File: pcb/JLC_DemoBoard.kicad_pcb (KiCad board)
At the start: 2 copper layers, 40.6 x 40.6 mm, 3 parts

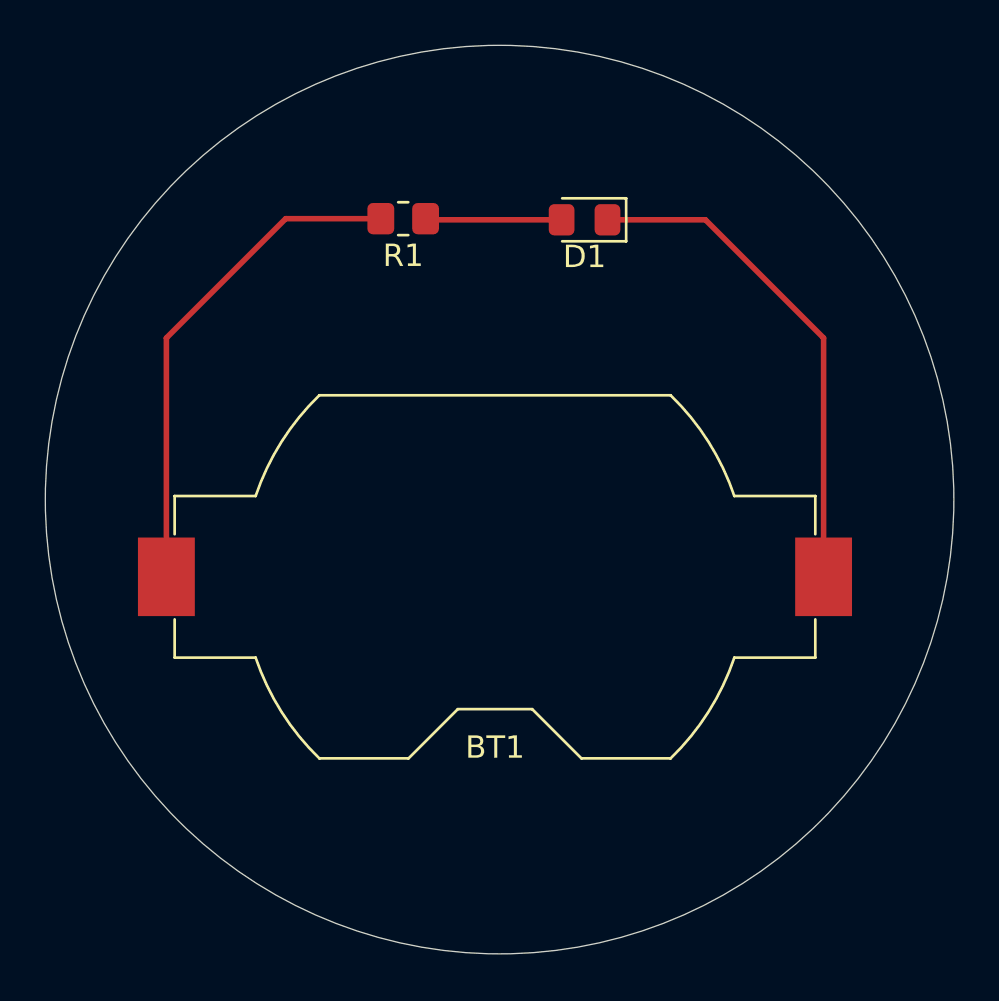
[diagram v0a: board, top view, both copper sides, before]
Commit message: Changed battery footprint
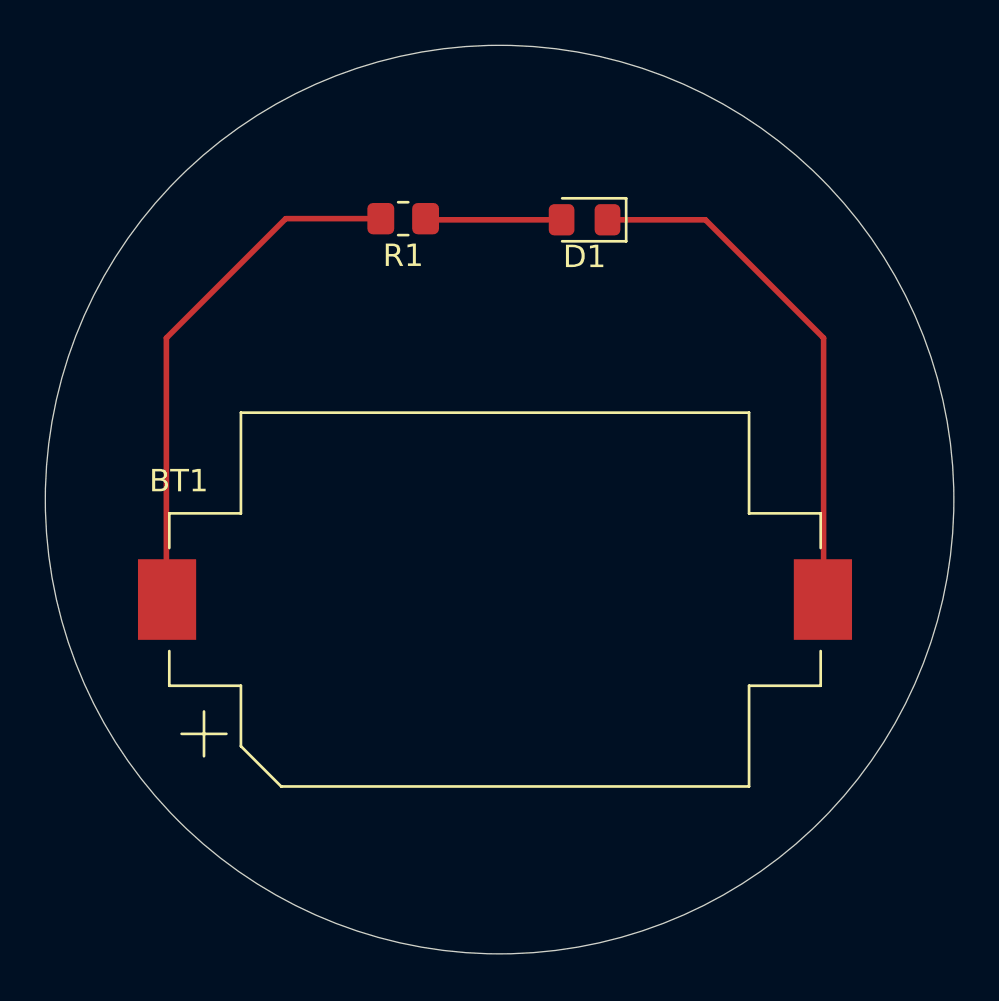
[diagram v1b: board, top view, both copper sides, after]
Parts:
- BT1: footprint Battery:BatteryHolder_Keystone_1058_1x2032 -> LCSC_Parts:BatteryHolder_2032
- turned BT1 to 180 degrees

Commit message: Added GND planes
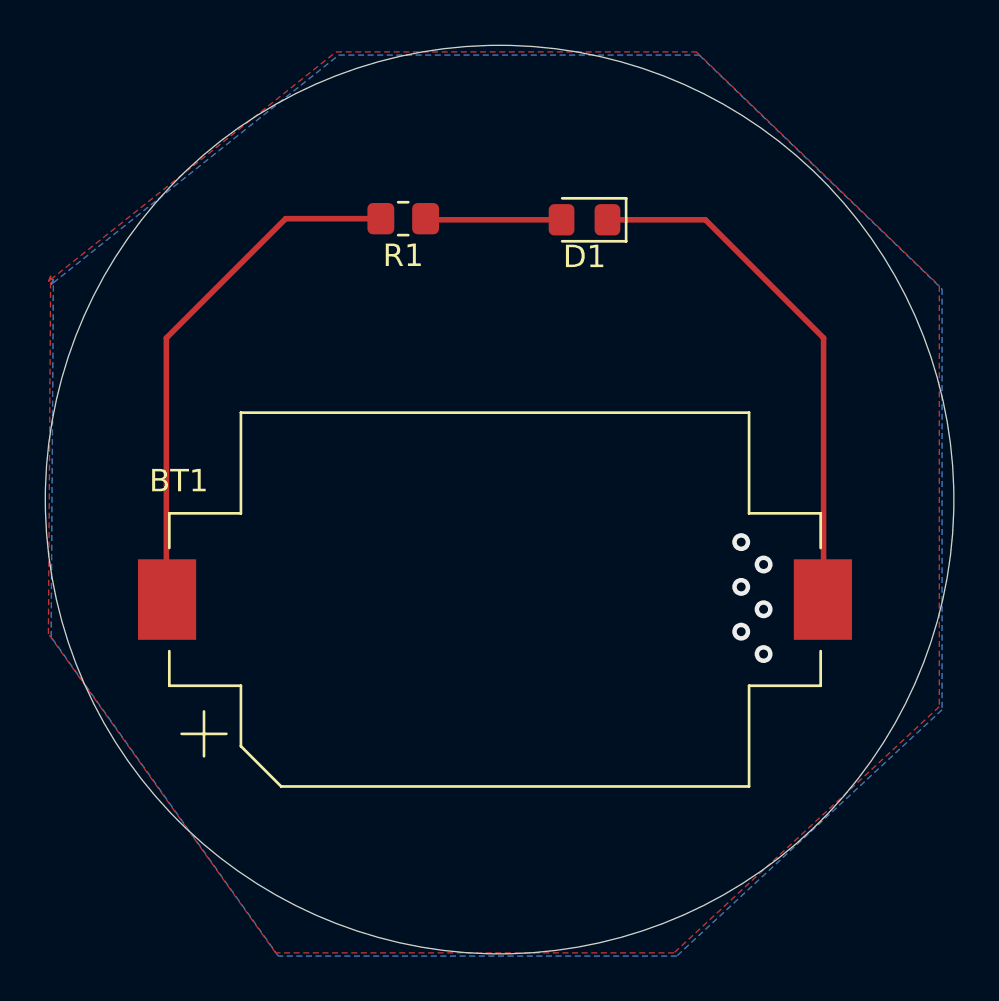
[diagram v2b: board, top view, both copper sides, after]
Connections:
- net Net-(BT1-Pad1) renamed VCC
- net Net-(BT1-Pad2) renamed GND
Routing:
- net GND: vias 0 -> 6
- added copper zone on B.Cu, net GND
- added copper zone on F.Cu, net GND
